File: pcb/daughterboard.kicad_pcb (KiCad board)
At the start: 2 copper layers, 22 x 31.3 mm, 51 parts, among them J1 USB_C_Receptacle_USB2.0, J2 Conn_01x02_Female, J3 Conn_01x02_Female, J4 USB_C_Receptacle_USB2.0, J5 Conn_01x02_Female, J6 Conn_01x02_Female

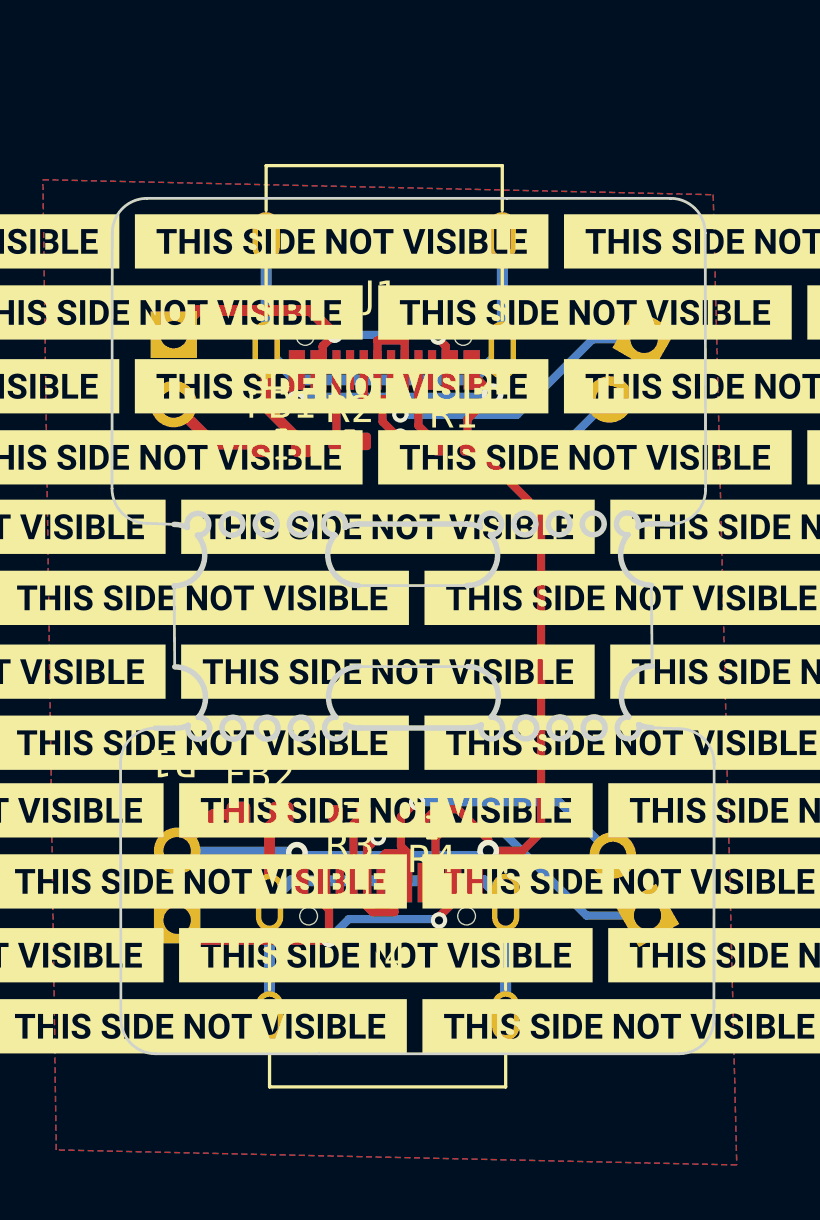
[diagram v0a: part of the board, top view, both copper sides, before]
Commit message: mid mount footprint and placement
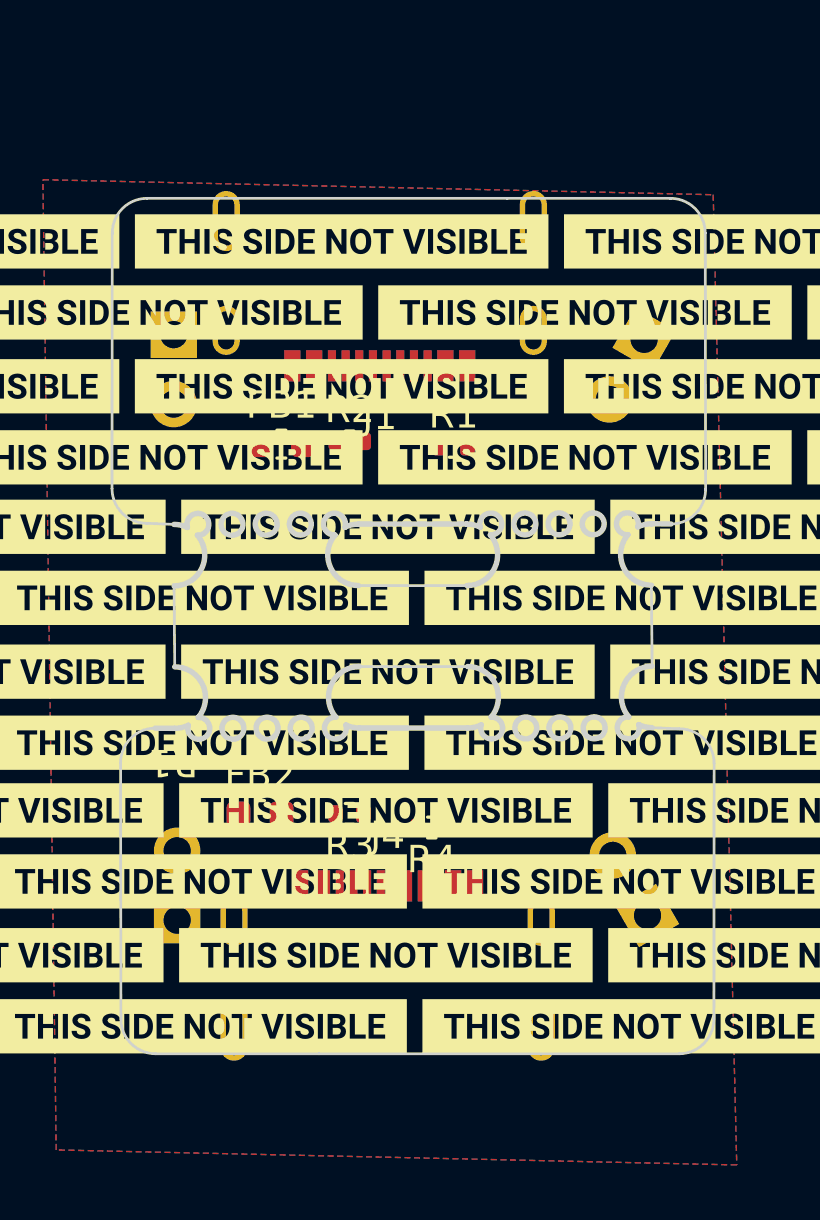
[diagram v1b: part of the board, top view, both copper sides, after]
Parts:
- J1, J4: footprint Library:C167321 -> Library:HRO-TYPE-C-31-M-13
- moved J1 6.82 mm to (34.8, 74.9)
- moved J4 6.79 mm to (35.1, 108.8)
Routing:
- net GND: track 58.4 -> 0.00 mm, vias 4 -> 0
- net Net-(FB1-Pad2): track 21.8 -> 0.00 mm
- net Net-(FB2-Pad2): track 21.0 -> 0.00 mm
- net Net-(J4-PadA7): track 16.1 -> 0.00 mm, vias 1 -> 0
- net Net-(J1-PadA7): track 14.9 -> 0.00 mm, vias 1 -> 0
- net Net-(J4-PadA4): track 14.0 -> 0.00 mm, vias 2 -> 0
- net Net-(J4-PadA6): track 13.3 -> 0.00 mm, vias 1 -> 0
- net Net-(J1-PadA4): track 13.3 -> 0.00 mm, vias 2 -> 0
- net Net-(J1-PadA6): track 13.1 -> 0.00 mm, vias 1 -> 0
- net Net-(J1-PadA5): track 3.14 -> 0.00 mm
- net Net-(J4-PadA5): track 2.67 -> 0.00 mm
- net Net-(J1-PadB5): track 2.62 -> 0.00 mm
- net Net-(J4-PadB5): track 2.17 -> 0.00 mm

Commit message: routing
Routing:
- net Net-(FB1-Pad2): track 0.00 -> 25.7 mm
- net GND: track 0.00 -> 19.7 mm, vias 0 -> 2
- net Net-(J1-PadA7): track 0.00 -> 14.8 mm, vias 0 -> 1
- net Net-(J1-PadA4): track 0.00 -> 13.5 mm, vias 0 -> 2
- net Net-(J1-PadA6): track 0.00 -> 13.3 mm, vias 0 -> 1
- net Net-(J1-PadA5): track 0.00 -> 3.35 mm
- net Net-(J1-PadB5): track 0.00 -> 2.82 mm

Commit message: edge cuts
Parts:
- moved kibuzzard-6284F97C 93.3 mm to (151.3, 88.2)
- moved kibuzzard-6284F97C 93.3 mm to (121.6, 93.3)
- moved kibuzzard-6284F97C 93.3 mm to (137.2, 103.7)
- moved kibuzzard-6284F97C 93.3 mm to (111.0, 85.6)
- moved kibuzzard-6284F97C 93.3 mm to (151.3, 82.9)
- moved kibuzzard-6284F97C 93.3 mm to (112.7, 90.7)
- moved kibuzzard-6284F97C 93.3 mm to (142.4, 85.6)
- moved kibuzzard-6284F97C 93.3 mm to (128.3, 101.1)
- moved kibuzzard-6284F97C 93.3 mm to (112.6, 106.4)
- moved kibuzzard-6284F97C 93.3 mm to (144.0, 101.1)
- moved kibuzzard-6284F97C 93.3 mm to (128.3, 106.4)
- moved kibuzzard-6284F97C 93.3 mm to (152.9, 109.0)
- moved kibuzzard-6284F97C 93.3 mm to (121.5, 109.0)
- moved kibuzzard-6284F97C 93.3 mm to (137.3, 98.6)
- moved kibuzzard-6284F97C 93.3 mm to (144.1, 96.0)
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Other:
- outline, holes or cut-outs redrawn

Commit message: edge cuts
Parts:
- moved FB1 0.80 mm to (30.4, 85.2)
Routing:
- net Net-(FB2-Pad2): track 0.00 -> 21.7 mm
- net GND: track 19.7 -> 6.10 mm, vias 2 -> 0
- net Net-(FB1-Pad2): track 25.7 -> 26.9 mm
- net Net-(J1-PadA4): track 13.5 -> 14.4 mm
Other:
- board size 22 x 31.3 mm -> 22 x 32.5 mm

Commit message: routing
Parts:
- moved kibuzzard-6284F97C 93.2 mm to (17.8, 83.2)
- moved kibuzzard-6284F97C 93.2 mm to (58.1, 80.5)
- moved kibuzzard-6284F97C 93.2 mm to (49.2, 83.2)
- moved kibuzzard-6284F97C 93.2 mm to (35.1, 98.7)
- moved kibuzzard-6284F97C 93.2 mm to (35.1, 104.0)
- moved kibuzzard-6284F97C 93.2 mm to (59.7, 106.6)
- moved kibuzzard-6284F97C 93.2 mm to (44.1, 96.2)
- moved kibuzzard-6284F97C 93.2 mm to (50.9, 93.6)
- moved kibuzzard-6284F97C 93.2 mm to (42.4, 85.8)
- moved kibuzzard-6284F97C 93.2 mm to (33.5, 83.2)
- moved kibuzzard-6284F97C 93.2 mm to (28.4, 96.2)
- moved kibuzzard-6284F97C 93.2 mm to (33.5, 77.9)
- moved kibuzzard-6284F97C 93.2 mm to (26.7, 85.8)
- moved kibuzzard-6284F97C 93.2 mm to (59.8, 90.9)
- moved kibuzzard-6284F97C 93.2 mm to (58.1, 85.8)
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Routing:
- net Net-(J4-PadA7): track 0.00 -> 22.1 mm, vias 0 -> 1
- net Net-(J4-PadA6): track 0.00 -> 17.0 mm, vias 0 -> 2
- net Net-(J4-PadA4): track 0.00 -> 16.9 mm, vias 0 -> 2
- net Net-(FB2-Pad2): track 21.7 -> 26.5 mm
- net Net-(J4-PadA5): track 0.00 -> 4.76 mm
- net Net-(J1-PadA6): track 13.3 -> 17.2 mm, vias 1 -> 2
- net Net-(J1-PadA4): track 14.4 -> 17.9 mm
- net Net-(J4-PadB5): track 0.00 -> 3.46 mm
- net GND: track 6.10 -> 2.96 mm
- net Net-(J1-PadA7): track 14.8 -> 17.9 mm
- net Net-(J1-PadB5): track 2.82 -> 3.54 mm

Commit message: DRC
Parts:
- moved kibuzzard-6284F97C 57.0 mm to (71.2, 63.4)
- moved kibuzzard-6284F97C 57.0 mm to (111.5, 66.0)
- moved kibuzzard-6284F97C 57.0 mm to (81.8, 71.1)
- moved kibuzzard-6284F97C 57.0 mm to (97.5, 81.5)
- moved kibuzzard-6284F97C 57.0 mm to (72.9, 68.5)
- moved kibuzzard-6284F97C 57.0 mm to (102.6, 63.4)
- moved kibuzzard-6284F97C 57.0 mm to (88.6, 78.9)
- moved kibuzzard-6284F97C 57.0 mm to (72.9, 84.2)
- moved kibuzzard-6284F97C 57.0 mm to (104.3, 78.9)
- moved kibuzzard-6284F97C 57.0 mm to (72.9, 78.9)
- moved kibuzzard-6284F97C 57.0 mm to (81.8, 86.8)
- moved kibuzzard-6284F97C 57.0 mm to (72.9, 73.8)
- moved kibuzzard-6284F97C 57.0 mm to (81.8, 81.5)
- moved kibuzzard-6284F97C 57.0 mm to (95.8, 66.0)
- moved kibuzzard-6284F97C 57.0 mm to (80.2, 60.7)
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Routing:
- net GND: track 2.96 -> 30.7 mm, vias 0 -> 6
- net Net-(J4-PadA6): track 17.0 -> 13.7 mm
- net Net-(FB1-Pad2): track 26.9 -> 23.9 mm
- net Net-(FB2-Pad2): track 26.5 -> 23.6 mm
- net Net-(J1-PadB5): track 3.54 -> 1.72 mm
- net Net-(J4-PadA5): track 4.76 -> 3.05 mm
- net Net-(J4-PadA4): track 16.9 -> 15.5 mm
- net Net-(J4-PadB5): track 3.46 -> 2.47 mm
- net Net-(J1-PadA4): track 17.9 -> 17.0 mm
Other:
- board text added: "0.2"
- board text removed: "0.1a"
